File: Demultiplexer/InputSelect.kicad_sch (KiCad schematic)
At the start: 2 parts, among them U201 74HC74

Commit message: Working on input stage
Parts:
- added C201: 100nF, Capacitor_THT:C_Disc_D5.0mm_W2.5mm_P5.00mm, symbol Device:C
- added C203, C204: 10u, Capacitor_THT:CP_Radial_D4.0mm_P1.50mm, symbol Device:C_Polarized
- added C205: 10u, symbol Device:C_Polarized
- added D201, D202: LED, LED_THT:LED_D5.0mm, symbol Device:LED
- added R201, R202, R203, R204: 22k, Resistor_THT:R_Axial_DIN0207_L6.3mm_D2.5mm_P7.62mm_Horizontal, symbol Device:R
- added R205, R206: 4k7, Resistor_THT:R_Axial_DIN0207_L6.3mm_D2.5mm_P7.62mm_Horizontal, symbol Device:R
- added R207: 1k, Resistor_THT:R_Axial_DIN0207_L6.3mm_D2.5mm_P7.62mm_Horizontal, symbol Device:R
- added R208: 100k, Resistor_THT:R_Axial_DIN0207_L6.3mm_D2.5mm_P7.62mm_Horizontal, symbol Device:R
- added SW201, SW202: SW_Push_Dual, Button_Switch_THT:SW_PUSH_6mm_H4.3mm, symbol Switch:SW_Push_Dual
- added U201: 74HC14, symbol 74xx:74HC14
- U202: renamed from U201; footprint (none) -> Package_DIP:DIP-14_W7.62mm_Socket
- renumbered C201 to C202
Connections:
- net +5V: now also U202.10 (~{S}), U202.4 (~{S}), C201.2, R201.1, R202.1, R207.1, U201.14 (VCC)
- net GND: now also C201.1, C203.2, C204.2, C205.2, R205.2, R206.2, R208.2, SW201.2, SW201.4, SW202.2, SW202.4, U201.11, U201.3, U201.7 (GND), U201.9
- net at U202.11 (C): now also U201.12
- net at U202.12 (D): now also U202.8 (~{Q})
- net ~{RESET}: now reaches U202.13 (~{R})
- net ~{RESET}: now also U202.1 (~{R}), C205.1, R207.2, R208.1
- net a_{1}: now reaches U202.9 (Q)
- net a_{1}: now also D202.2 (A)
- net at U202.2 (D): now also U202.6 (~{Q})
- net at U202.3 (C): now also U201.2
- net a_{0}: now reaches U202.5 (Q)
- net a_{0}: now also D201.2 (A)
- new net: D202.1 (K), R206.1
- new net: C203.1, R203.2, U201.1
- new net: R201.2, R203.1, SW201.1, SW201.3
- new net: D201.1 (K), R205.1
- new net: R202.2, R204.1, SW202.1, SW202.3
- new net: C204.1, R204.2, U201.13
- no-connect marks 0 -> 4
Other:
- moved on the sheet: U202B

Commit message: Working on decoder stage
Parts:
- C205: footprint (none) -> Capacitor_THT:CP_Radial_D4.0mm_P1.50mm
- SW201, SW202: symbol Switch:SW_Push_Dual -> Switch:SW_Push
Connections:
- net GND: no longer SW201.4, SW202.4
- net at R201.2, R203.1, SW201.1: no longer SW201.3
- net at R202.2, R204.1, SW202.1: no longer SW202.3
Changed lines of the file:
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@@
   (junction (at 195.58 55.88) (diameter 0) (color 0 0 0 0)
   )
-  (junction (at 100.33 72.39) (diameter 0) (color 0 0 0 0)
-  )
   (junction (at 74.93 156.21) (diameter 0) (color 0 0 0 0)
   )
@@
   (junction (at 17.78 184.15) (diameter 0) (color 0 0 0 0)
   )
-  (junction (at 90.17 72.39) (diameter 0) (color 0 0 0 0)
-  )
-  (junction (at 101.6 120.65) (diameter 0) (color 0 0 0 0)
-  )
   (junction (at 107.95 72.39) (diameter 0) (color 0 0 0 0)
   )
@@
   )
   (junction (at 259.08 45.72) (diameter 0) (color 0 0 0 0)
-  )
-  (junction (at 91.44 120.65) (diameter 0) (color 0 0 0 0)
   )
   (no_connect (at 35.56 135.89))
@@
     (stroke (width 0) (type default) (color 0 0 0 0))
   )
-  (wire (pts (xy 90.17 69.85) (xy 90.17 72.39))
-    (stroke (width 0) (type default) (color 0 0 0 0))
-  )
   (wire (pts (xy 163.83 71.12) (xy 168.91 71.12))
     (stroke (width 0) (type default) (color 0 0 0 0))
@@
     (stroke (width 0) (type default) (color 0 0 0 0))
   )
-  (wire (pts (xy 90.17 72.39) (xy 90.17 74.93))
-    (stroke (width 0) (type default) (color 0 0 0 0))
-  )
   (wire (pts (xy 102.87 58.42) (xy 107.95 58.42))
     (stroke (width 0) (type default) (color 0 0 0 0))
@@
     (stroke (width 0) (type default) (color 0 0 0 0))
   )
-  (wire (pts (xy 91.44 118.11) (xy 91.44 120.65))
-    (stroke (width 0) (type default) (color 0 0 0 0))
-  )
   (wire (pts (xy 195.58 104.14) (xy 209.55 104.14))
     (stroke (width 0) (type default) (color 0 0 0 0))
@@
     (stroke (width 0) (type default) (color 0 0 0 0))
   )
-  (wire (pts (xy 91.44 120.65) (xy 91.44 123.19))
-    (stroke (width 0) (type default) (color 0 0 0 0))
-  )
   (wire (pts (xy 259.08 45.72) (xy 259.08 48.26))
     (stroke (width 0) (type default) (color 0 0 0 0))
@@
     (stroke (width 0) (type default) (color 0 0 0 0))
   )
-  (wire (pts (xy 100.33 69.85) (xy 100.33 72.39))
-    (stroke (width 0) (type default) (color 0 0 0 0))
-  )
-  (wire (pts (xy 100.33 72.39) (xy 100.33 74.93))
-    (stroke (width 0) (type default) (color 0 0 0 0))
-  )
   (wire (pts (xy 156.21 55.88) (xy 143.51 55.88))
     (stroke (width 0) (type default) (color 0 0 0 0))
@@
     (stroke (width 0) (type default) (color 0 0 0 0))
   )
-  (wire (pts (xy 101.6 120.65) (xy 101.6 123.19))
-    (stroke (width 0) (type default) (color 0 0 0 0))
-  )
   (wire (pts (xy 17.78 168.91) (xy 17.78 152.4))
     (stroke (width 0) (type default) (color 0 0 0 0))
@@
   )
   (wire (pts (xy 17.78 187.96) (xy 17.78 184.15))
-    (stroke (width 0) (type default) (color 0 0 0 0))
-  )
-  (wire (pts (xy 101.6 118.11) (xy 101.6 120.65))
     (stroke (width 0) (type default) (color 0 0 0 0))
   )
@@
       (effects (font (size 1.27 1.27)) (justify left))
     )
-    (property "Footprint" "" (id 2) (at 272.7452 43.18 0)
+    (property "Footprint" "Capacitor_THT:CP_Radial_D4.0mm_P1.50mm" (id 2) (at 272.7452 43.18 0)
       (effects (font (size 1.27 1.27)) hide)
     )
@@
     (pin "1")
   )
-  (symbol (lib_id "Switch:SW_Push_Dual") (at 95.25 69.85 0) (unit 1)
-    (in_bom yes) (on_board yes) (fields_autoplaced)
-    (property "Reference" "SW201" (id 0) (at 95.25 62.23 0))
-    (property "Value" "SW_Push_Dual" (id 1) (at 95.25 64.77 0))
-    (property "Footprint" "Button_Switch_THT:SW_PUSH_6mm_H4.3mm" (id 2) (at 95.25 64.77 0)
-      (effects (font (size 1.27 1.27)) hide)
-    )
-    (property "Datasheet" "~" (id 3) (at 95.25 64.77 0)
-      (effects (font (size 1.27 1.27)) hide)
-    )
-    (pin "1")
-    (pin "2")
-    (pin "3")
-    (pin "4")
+  (symbol (lib_id "Switch:SW_Push") (at 95.25 72.39 0) (unit 1)
+    (in_bom yes) (on_board yes)
+    (property "Reference" "SW201" (id 0) (at 95.25 64.77 0))
+    (property "Value" "SW_Push_Dual" (id 1) (at 95.25 67.31 0))
+    (property "Footprint" "Button_Switch_THT:SW_PUSH_6mm_H4.3mm" (id 2) (at 95.25 67.31 0)
+      (effects (font (size 1.27 1.27)) hide)
+    )
+    (property "Datasheet" "~" (id 3) (at 95.25 67.31 0)
+      (effects (font (size 1.27 1.27)) hide)
+    )
+    (pin "1")
+    (pin "2")
   )
   (symbol (lib_id "74xx:74HC14") (at 27.94 135.89 0) (unit 2)
@@
     (pin "2")
   )
-  (symbol (lib_id "Switch:SW_Push_Dual") (at 96.52 118.11 0) (unit 1)
-    (in_bom yes) (on_board yes) (fields_autoplaced)
-    (property "Reference" "SW202" (id 0) (at 96.52 110.49 0))
-    (property "Value" "SW_Push_Dual" (id 1) (at 96.52 113.03 0))
-    (property "Footprint" "Button_Switch_THT:SW_PUSH_6mm_H4.3mm" (id 2) (at 96.52 113.03 0)
-      (effects (font (size 1.27 1.27)) hide)
-    )
-    (property "Datasheet" "~" (id 3) (at 96.52 113.03 0)
-      (effects (font (size 1.27 1.27)) hide)
-    )
-    (pin "1")
-    (pin "2")
-    (pin "3")
-    (pin "4")
+  (symbol (lib_id "Switch:SW_Push") (at 96.52 120.65 0) (unit 1)
+    (in_bom yes) (on_board yes) (fields_autoplaced)
+    (property "Reference" "SW202" (id 0) (at 96.52 113.03 0))
+    (property "Value" "SW_Push_Dual" (id 1) (at 96.52 115.57 0))
+    (property "Footprint" "Button_Switch_THT:SW_PUSH_6mm_H4.3mm" (id 2) (at 96.52 115.57 0)
+      (effects (font (size 1.27 1.27)) hide)
+    )
+    (property "Datasheet" "~" (id 3) (at 96.52 115.57 0)
+      (effects (font (size 1.27 1.27)) hide)
+    )
+    (pin "1")
+    (pin "2")
   )
   (symbol (lib_id "74xx:74HC14") (at 27.94 152.4 0) (unit 3)

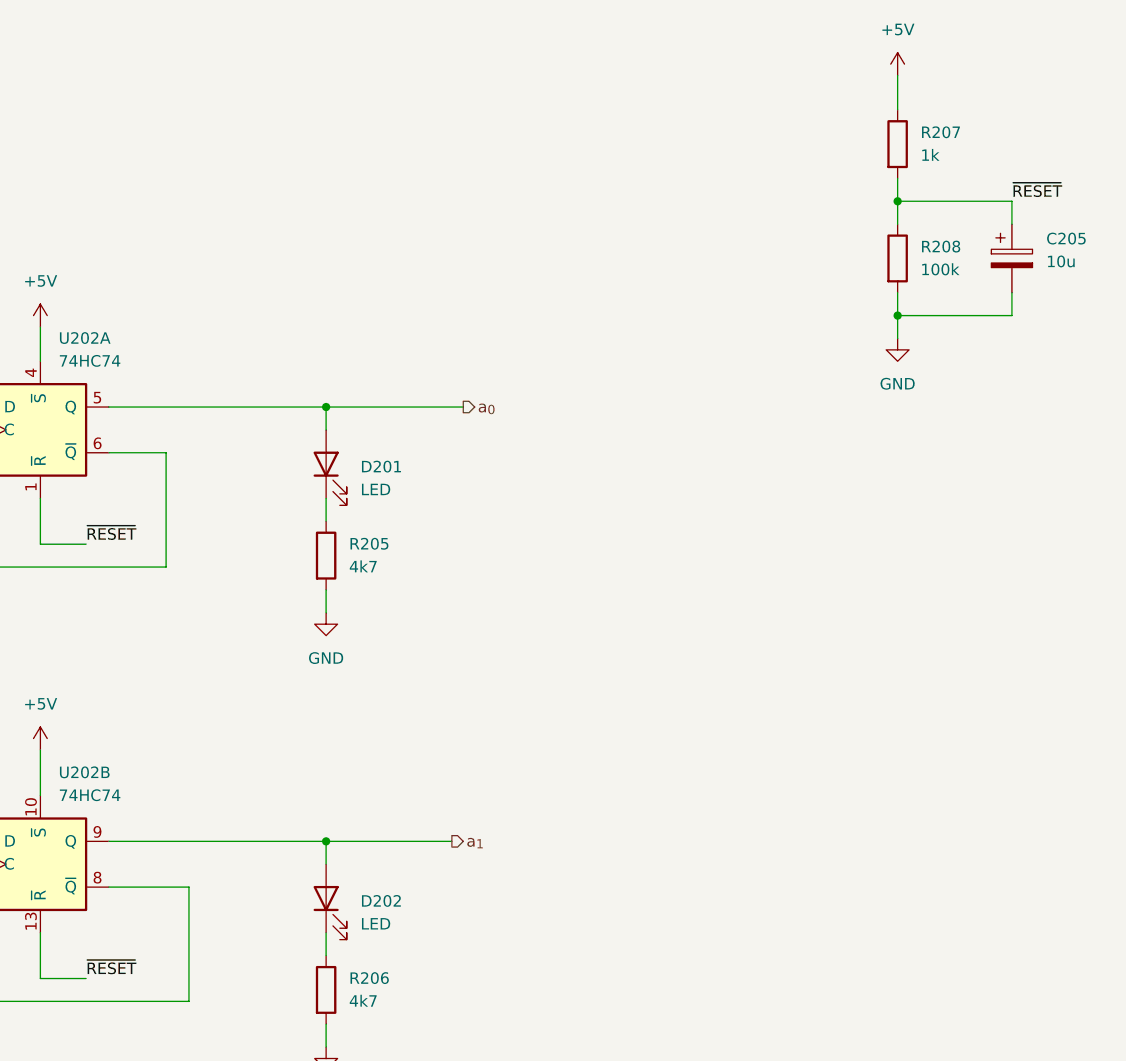
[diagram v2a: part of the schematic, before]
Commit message: Rethinking NOT gates and starting on output
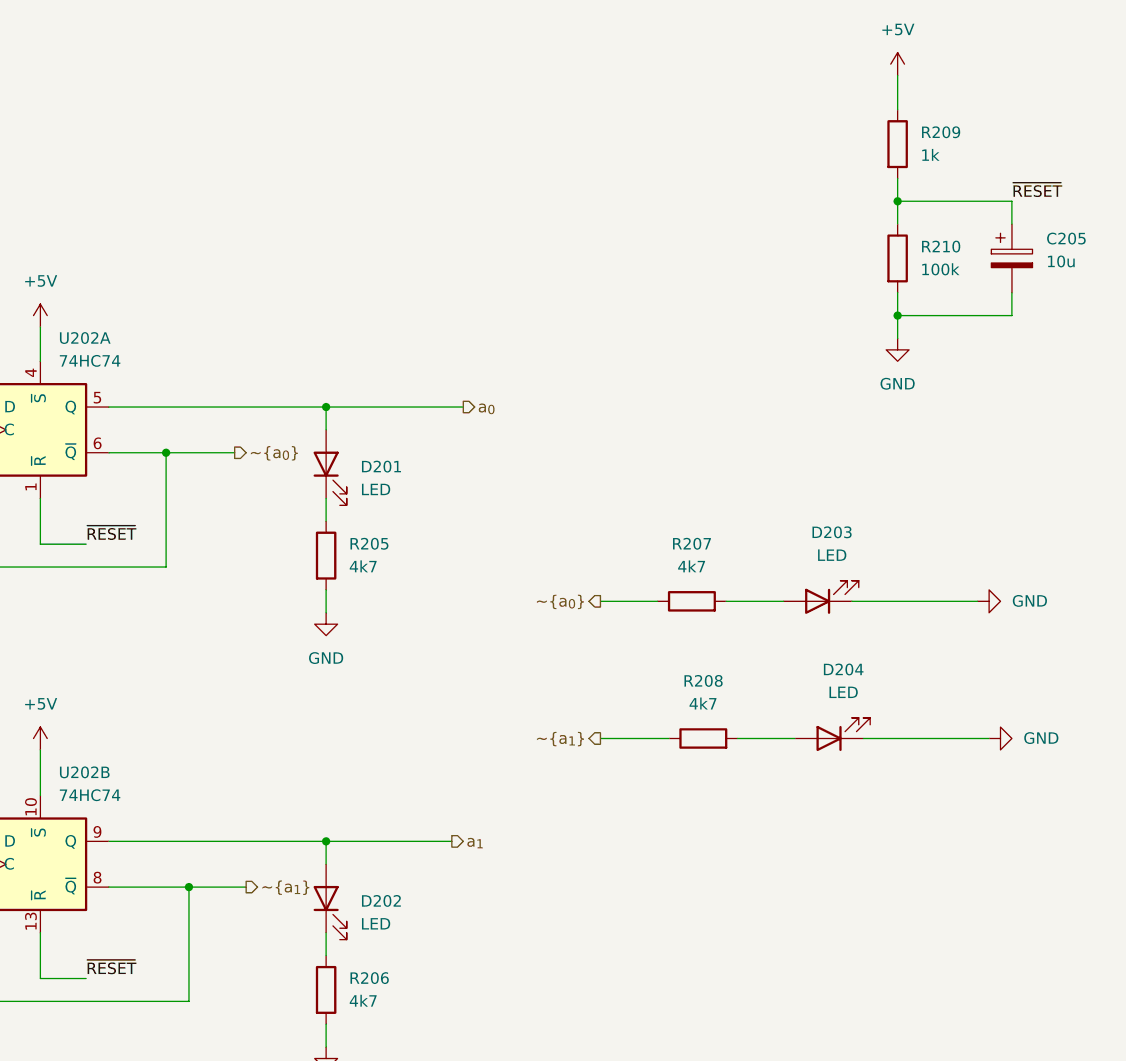
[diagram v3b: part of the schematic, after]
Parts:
- added D203, D204: LED, LED_THT:LED_D3.0mm, symbol Device:LED
- added R207, R208: 4k7, Resistor_THT:R_Axial_DIN0207_L6.3mm_D2.5mm_P7.62mm_Horizontal, symbol Device:R
- renumbered R207 to R209, R208 to R210
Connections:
- net GND: now also D203.1 (K), D204.1 (K)
- net ~{a_{1}}: now reaches U202.12 (D), U202.8 (~{Q})
- net ~{a_{1}}: now also R208.1
- net ~{a_{0}}: now reaches U202.2 (D), U202.6 (~{Q})
- net ~{a_{0}}: now also R207.1
- new net: D203.2 (A), R207.2
- new net: D204.2 (A), R208.2
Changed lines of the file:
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@@
   (junction (at 195.58 55.88) (diameter 0) (color 0 0 0 0)
   )
+  (junction (at 180.34 109.22) (diameter 0) (color 0 0 0 0)
+  )
   (junction (at 74.93 156.21) (diameter 0) (color 0 0 0 0)
   )
@@
   )
   (junction (at 17.78 168.91) (diameter 0) (color 0 0 0 0)
+  )
+  (junction (at 177.8 60.96) (diameter 0) (color 0 0 0 0)
   )
   (junction (at 109.22 106.68) (diameter 0) (color 0 0 0 0)
@@
     (stroke (width 0) (type default) (color 0 0 0 0))
   )
+  (wire (pts (xy 177.8 60.96) (xy 185.42 60.96))
+    (stroke (width 0) (type default) (color 0 0 0 0))
+  )
   (wire (pts (xy 106.68 177.8) (xy 106.68 185.42))
     (stroke (width 0) (type default) (color 0 0 0 0))
@@
     (stroke (width 0) (type default) (color 0 0 0 0))
   )
+  (wire (pts (xy 226.06 92.71) (xy 233.68 92.71))
+    (stroke (width 0) (type default) (color 0 0 0 0))
+  )
   (wire (pts (xy 130.81 158.75) (xy 130.81 162.56))
     (stroke (width 0) (type default) (color 0 0 0 0))
@@
     (stroke (width 0) (type default) (color 0 0 0 0))
   )
+  (wire (pts (xy 255.27 92.71) (xy 269.24 92.71))
+    (stroke (width 0) (type default) (color 0 0 0 0))
+  )
   (wire (pts (xy 107.95 69.85) (xy 107.95 72.39))
     (stroke (width 0) (type default) (color 0 0 0 0))
@@
     (stroke (width 0) (type default) (color 0 0 0 0))
   )
+  (wire (pts (xy 240.03 77.47) (xy 246.38 77.47))
+    (stroke (width 0) (type default) (color 0 0 0 0))
+  )
   (wire (pts (xy 52.07 156.21) (xy 52.07 168.91))
     (stroke (width 0) (type default) (color 0 0 0 0))
@@
     (stroke (width 0) (type default) (color 0 0 0 0))
   )
+  (wire (pts (xy 180.34 109.22) (xy 186.69 109.22))
+    (stroke (width 0) (type default) (color 0 0 0 0))
+  )
   (wire (pts (xy 180.34 121.92) (xy 180.34 109.22))
     (stroke (width 0) (type default) (color 0 0 0 0))
@@
     (stroke (width 0) (type default) (color 0 0 0 0))
   )
+  (wire (pts (xy 254 77.47) (xy 267.97 77.47))
+    (stroke (width 0) (type default) (color 0 0 0 0))
+  )
   (wire (pts (xy 87.63 43.18) (xy 87.63 46.99))
     (stroke (width 0) (type default) (color 0 0 0 0))
@@
     (stroke (width 0) (type default) (color 0 0 0 0))
   )
+  (wire (pts (xy 226.06 77.47) (xy 232.41 77.47))
+    (stroke (width 0) (type default) (color 0 0 0 0))
+  )
   (wire (pts (xy 88.9 106.68) (xy 88.9 120.65))
     (stroke (width 0) (type default) (color 0 0 0 0))
@@
   )
   (wire (pts (xy 163.83 119.38) (xy 163.83 114.3))
+    (stroke (width 0) (type default) (color 0 0 0 0))
+  )
+  (wire (pts (xy 241.3 92.71) (xy 247.65 92.71))
     (stroke (width 0) (type default) (color 0 0 0 0))
   )
@@
     (effects (font (size 1.27 1.27)) (justify left bottom))
   )
+  (hierarchical_label "~{a_{0}}" (shape output) (at 185.42 60.96 0)
+    (effects (font (size 1.27 1.27)) (justify left))
+  )
   (hierarchical_label "a_{0}" (shape output) (at 210.82 55.88 0)
     (effects (font (size 1.27 1.27)) (justify left))
   )
+  (hierarchical_label "~{a_{0}}" (shape output) (at 226.06 77.47 180)
+    (effects (font (size 1.27 1.27)) (justify right))
+  )
+  (hierarchical_label "~{a_{1}}" (shape output) (at 186.69 109.22 0)
+    (effects (font (size 1.27 1.27)) (justify left))
+  )
   (hierarchical_label "a_{1}" (shape output) (at 209.55 104.14 0)
     (effects (font (size 1.27 1.27)) (justify left))
+  )
+  (hierarchical_label "~{a_{1}}" (shape output) (at 226.06 92.71 180)
+    (effects (font (size 1.27 1.27)) (justify right))
   )
   (symbol (lib_id "power:GND") (at 74.93 185.42 0) (unit 1)
@@
     (pin "7")
   )
+  (symbol (lib_id "Device:R") (at 236.22 77.47 90) (unit 1)
+    (in_bom yes) (on_board yes) (fields_autoplaced)
+    (property "Reference" "R207" (id 0) (at 236.22 71.12 90))
+    (property "Value" "4k7" (id 1) (at 236.22 73.66 90))
+    (property "Footprint" "Resistor_THT:R_Axial_DIN0207_L6.3mm_D2.5mm_P7.62mm_Horizontal" (id 2) (at 236.22 79.248 90)
+      (effects (font (size 1.27 1.27)) hide)
+    )
+    (property "Datasheet" "~" (id 3) (at 236.22 77.47 0)
+      (effects (font (size 1.27 1.27)) hide)
+    )
+    (pin "1")
+    (pin "2")
+  )
   (symbol (lib_id "power:GND") (at 109.22 123.19 0) (unit 1)
     (in_bom yes) (on_board yes) (fields_autoplaced)
@@
     (pin "1")
   )
+  (symbol (lib_id "power:GND") (at 267.97 77.47 90) (unit 1)
+    (in_bom yes) (on_board yes) (fields_autoplaced)
+    (property "Reference" "#PWR0216" (id 0) (at 274.32 77.47 0)
+      (effects (font (size 1.27 1.27)) hide)
+    )
+    (property "Value" "GND" (id 1) (at 271.78 77.4699 90)
+      (effects (font (size 1.27 1.27)) (justify right))
+    )
+    (property "Footprint" "" (id 2) (at 267.97 77.47 0)
+      (effects (font (size 1.27 1.27)) hide)
+    )
+    (property "Datasheet" "" (id 3) (at 267.97 77.47 0)
+      (effects (font (size 1.27 1.27)) hide)
+    )
+    (pin "1")
+  )
   (symbol (lib_id "Switch:SW_Push") (at 95.25 72.39 0) (unit 1)
     (in_bom yes) (on_board yes)
@@
     (pin "7")
   )
+  (symbol (lib_id "Device:R") (at 237.49 92.71 90) (unit 1)
+    (in_bom yes) (on_board yes) (fields_autoplaced)
+    (property "Reference" "R208" (id 0) (at 237.49 86.36 90))
+    (property "Value" "4k7" (id 1) (at 237.49 88.9 90))
+    (property "Footprint" "Resistor_THT:R_Axial_DIN0207_L6.3mm_D2.5mm_P7.62mm_Horizontal" (id 2) (at 237.49 94.488 90)
+      (effects (font (size 1.27 1.27)) hide)
+    )
+    (property "Datasheet" "~" (id 3) (at 237.49 92.71 0)
+      (effects (font (size 1.27 1.27)) hide)
+    )
+    (pin "1")
+    (pin "2")
+  )
   (symbol (lib_id "Device:R") (at 195.58 72.39 0) (unit 1)
     (in_bom yes) (on_board yes) (fields_autoplaced)
@@
   (symbol (lib_id "Device:R") (at 259.08 39.37 0) (unit 1)
     (in_bom yes) (on_board yes) (fields_autoplaced)
-    (property "Reference" "R208" (id 0) (at 261.62 38.0999 0)
+    (property "Reference" "R210" (id 0) (at 261.62 38.0999 0)
       (effects (font (size 1.27 1.27)) (justify left))
     )
@@
     (pin "2")
   )
+  (symbol (lib_id "Device:LED") (at 250.19 77.47 180) (unit 1)
+    (in_bom yes) (on_board yes) (fields_autoplaced)
+    (property "Reference" "D203" (id 0) (at 251.7775 69.85 0))
+    (property "Value" "LED" (id 1) (at 251.7775 72.39 0))
+    (property "Footprint" "LED_THT:LED_D3.0mm" (id 2) (at 250.19 77.47 0)
+      (effects (font (size 1.27 1.27)) hide)
+    )
+    (property "Datasheet" "~" (id 3) (at 250.19 77.47 0)
+      (effects (font (size 1.27 1.27)) hide)
+    )
+    (pin "1")
+    (pin "2")
+  )
   (symbol (lib_id "power:+5V") (at 163.83 46.99 0) (unit 1)
     (in_bom yes) (on_board yes) (fields_autoplaced)
@@
     (pin "1")
     (pin "2")
+  )
+  (symbol (lib_id "Device:LED") (at 251.46 92.71 180) (unit 1)
+    (in_bom yes) (on_board yes) (fields_autoplaced)
+    (property "Reference" "D204" (id 0) (at 253.0475 85.09 0))
+    (property "Value" "LED" (id 1) (at 253.0475 87.63 0))
+    (property "Footprint" "LED_THT:LED_D3.0mm" (id 2) (at 251.46 92.71 0)
+      (effects (font (size 1.27 1.27)) hide)
+    )
+    (property "Datasheet" "~" (id 3) (at 251.46 92.71 0)
+      (effects (font (size 1.27 1.27)) hide)
+    )
+    (pin "1")
+    (pin "2")
+  )
+  (symbol (lib_id "power:GND") (at 269.24 92.71 90) (unit 1)
+    (in_bom yes) (on_board yes) (fields_autoplaced)
+    (property "Reference" "#PWR0217" (id 0) (at 275.59 92.71 0)
+      (effects (font (size 1.27 1.27)) hide)
+    )
+    (property "Value" "GND" (id 1) (at 273.05 92.7099 90)
+      (effects (font (size 1.27 1.27)) (justify right))
+    )
+    (property "Footprint" "" (id 2) (at 269.24 92.71 0)
+      (effects (font (size 1.27 1.27)) hide)
+    )
+    (property "Datasheet" "" (id 3) (at 269.24 92.71 0)
+      (effects (font (size 1.27 1.27)) hide)
+    )
+    (pin "1")
   )
   (symbol (lib_id "74xx:74HC14") (at 27.94 152.4 0) (unit 3)
@@
   (symbol (lib_id "Device:R") (at 259.08 26.67 0) (unit 1)
     (in_bom yes) (on_board yes) (fields_autoplaced)
-    (property "Reference" "R207" (id 0) (at 261.62 25.3999 0)
-      (effects (font (size 1.27 1.27)) (justify left))
-    )
+    (property "Reference" "R209" (id 0) (at 261.62 25.3999 0)
+      (effects (font (size 1.27 1.27)) (justify left))
+    )

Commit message: Finish roughing out board
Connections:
- net +5V: now also R201.2, R202.2; no longer R201.1, R202.1
- net at R203.1, SW201.1: now also R201.1; no longer R201.2
- net at R204.1, SW202.1: now also R202.1; no longer R202.2
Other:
- moved on the sheet: R201, R202
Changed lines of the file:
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@@
     (pin "1")
   )
-  (symbol (lib_id "Device:R") (at 88.9 99.06 0) (unit 1)
+  (symbol (lib_id "Device:R") (at 88.9 99.06 180) (unit 1)
     (in_bom yes) (on_board yes) (fields_autoplaced)
     (property "Reference" "R202" (id 0) (at 91.44 97.7899 0)
-      (effects (font (size 1.27 1.27)) (justify left))
+      (effects (font (size 1.27 1.27)) (justify right))
     )
     (property "Value" "22k" (id 1) (at 91.44 100.3299 0)
-      (effects (font (size 1.27 1.27)) (justify left))
+      (effects (font (size 1.27 1.27)) (justify right))
     )
-    (property "Footprint" "Resistor_THT:R_Axial_DIN0207_L6.3mm_D2.5mm_P7.62mm_Horizontal" (id 2) (at 87.122 99.06 90)
+    (property "Footprint" "Resistor_THT:R_Axial_DIN0207_L6.3mm_D2.5mm_P7.62mm_Horizontal" (id 2) (at 90.678 99.06 90)
       (effects (font (size 1.27 1.27)) hide)
     )
@@
     (pin "2")
   )
-  (symbol (lib_id "Device:R") (at 87.63 50.8 0) (unit 1)
+  (symbol (lib_id "Device:R") (at 87.63 50.8 180) (unit 1)
     (in_bom yes) (on_board yes) (fields_autoplaced)
     (property "Reference" "R201" (id 0) (at 90.17 49.5299 0)
-      (effects (font (size 1.27 1.27)) (justify left))
+      (effects (font (size 1.27 1.27)) (justify right))
     )
     (property "Value" "22k" (id 1) (at 90.17 52.0699 0)
-      (effects (font (size 1.27 1.27)) (justify left))
+      (effects (font (size 1.27 1.27)) (justify right))
     )
-    (property "Footprint" "Resistor_THT:R_Axial_DIN0207_L6.3mm_D2.5mm_P7.62mm_Horizontal" (id 2) (at 85.852 50.8 90)
+    (property "Footprint" "Resistor_THT:R_Axial_DIN0207_L6.3mm_D2.5mm_P7.62mm_Horizontal" (id 2) (at 89.408 50.8 90)
       (effects (font (size 1.27 1.27)) hide)
     )
